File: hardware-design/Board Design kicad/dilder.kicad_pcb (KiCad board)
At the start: 4 copper layers, 48 x 85 mm, 25 parts, among them J1 USB-C, J2 BAT, J3 ePaper-FPC, Q1 FS8205A, SW1 5-Way, U1 ESP32-S3-N16R8, U2 TP4056, U3 DW01A, U4 AMS1117-3.3, U6 MPU-6050

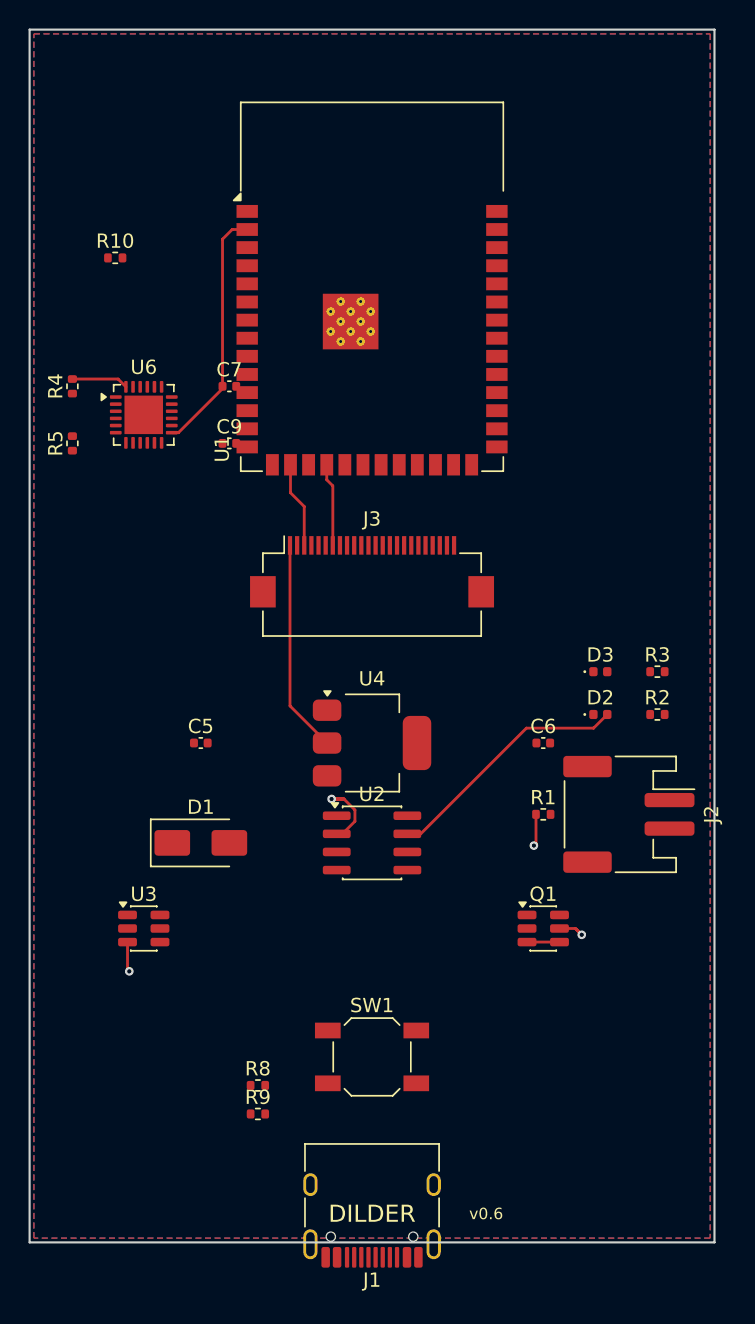
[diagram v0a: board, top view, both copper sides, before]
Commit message: Optimized PCB placement (45x80mm), blog post, docs update, Prompt #145
PCB v7: 45x80mm 4-layer board with research-informed placement.
ESP32-S3 antenna overhangs top edge, joystick+USB-C centered at bottom,
IMU left of module near I2C pins, JST-SH 8-pin ePaper connector,
power section spread in middle. 1 courtyard overlap, 0 edge violations.

Blog: "From RP2040 to ESP32-S3 — Designing the Dilder PCB"
README + home page updated with PCB design milestone.

Co-Authored-By: Claude Opus 4.6 (1M context) <noreply@anthropic.com>
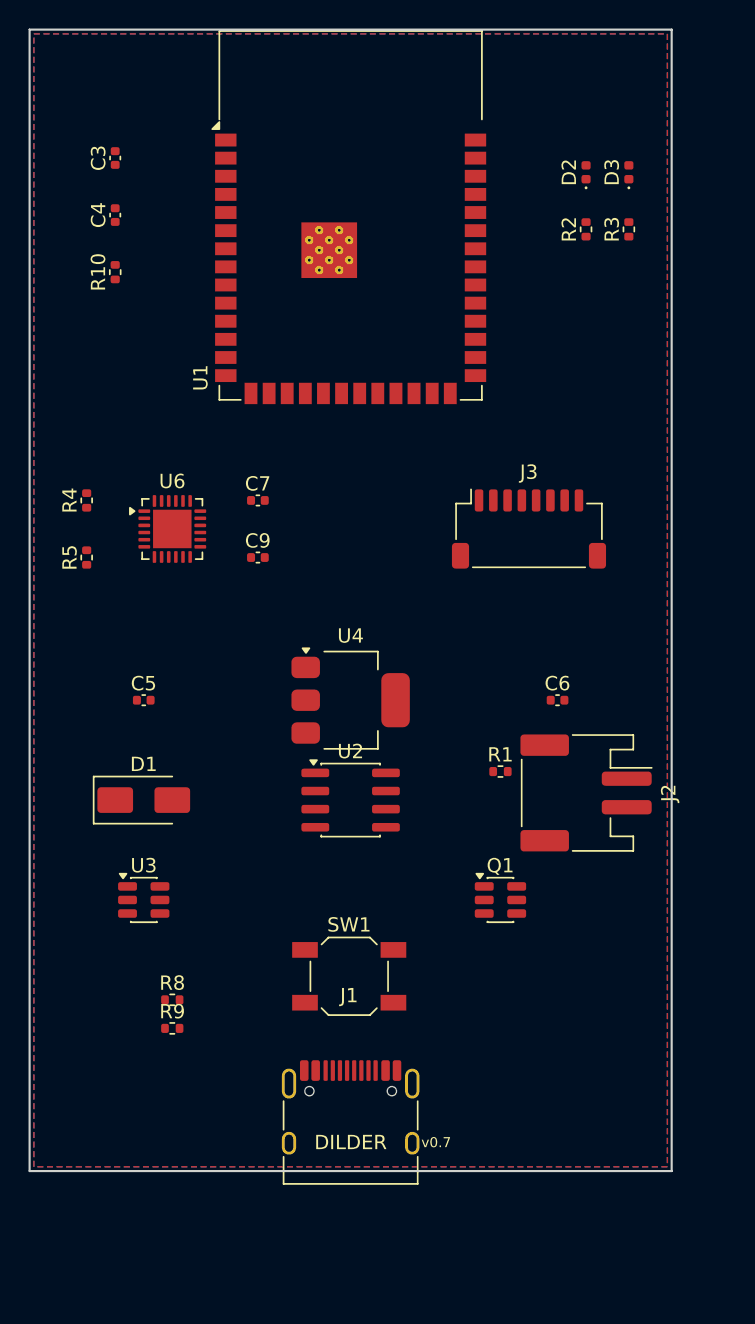
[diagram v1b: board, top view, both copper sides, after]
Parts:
- added C3: 100nF, C_0402_1005Metric, F.Cu at (106.0, 109.0)
- added C4: 10uF, C_0402_1005Metric, F.Cu at (106.0, 113.0)
- J3: value ePaper-FPC -> ePaper; footprint Hirose_FH12-24S-0.5SH_1x24-1MP_P0.50mm_Horizontal -> JST_SH_SM08B-SRSS-TB_1x08-1MP_P1.00mm_Horizontal
- moved D2 38.0 mm to (139.0, 110.0), turned to 90 degrees
- moved D3 35.1 mm to (142.0, 110.0), turned to 90 degrees
- moved R2 34.4 mm to (139.0, 114.0), turned to 90 degrees
- moved R3 31.1 mm to (142.0, 114.0), turned to 90 degrees
- moved J3 11.4 mm to (135.0, 135.0)
- moved R8 8.49 mm to (110.0, 168.0)
- moved R9 8.49 mm to (110.0, 170.0)
- moved C7 8.25 mm to (116.0, 133.0)
- moved C9 8.25 mm to (116.0, 137.0)
- moved U6 8.25 mm to (110.0, 135.0)
- moved R4 8.06 mm to (104.0, 133.0)
- moved R5 8.06 mm to (104.0, 137.0)
- moved SW1 5.87 mm to (122.4, 166.3)
- moved J1 5.22 mm to (122.5, 177.0), turned to 0 degrees
- moved U1 5.22 mm to (122.5, 113.0)
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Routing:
- net OC: track 39.5 -> 0.00 mm, vias 2 -> 0
- net 3V3: track 32.2 -> 0.00 mm
- net PROG: track 26.5 -> 0.00 mm, vias 2 -> 0
- net CHRG_OUT: track 17.5 -> 0.00 mm
- net EPD_MOSI: track 6.05 -> 0.00 mm
- net EPD_RST: track 5.83 -> 0.00 mm
- net I2C_SDA: track 3.98 -> 0.00 mm
- net CS_DRAIN: track 2.27 -> 0.00 mm
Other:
- board size 48 x 85 mm -> 45 x 80 mm
- board text added: "v0.7"
- board text removed: "v0.6"
